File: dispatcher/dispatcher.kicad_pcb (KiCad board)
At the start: 2 copper layers, 29 parts, among them J1 Conn_01x06_Female, J2 Conn_01x18, K1 HFD2_005-S-L2-D, K2 HFD2_005-S-L2-D, U1 INA3221_Module, U2 ULN2803A, U3 ULN2803A, U5 MCP2551-I-P, U6 ChinaBluePill-bluepill-D3_Boa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

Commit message: mainboard4 ready for production
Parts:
- added C1: C, Capacitor_THT:C_Disc_D3.4mm_W2.1mm_P2.50mm, F.Cu at (234.4, 139.7)
- added C2: C, Capacitor_THT:C_Disc_D3.4mm_W2.1mm_P2.50mm, F.Cu at (247.1, 139.7)
- R5: value R -> locked
- moved K2 140.0 mm to (252.1, 66.0), turned to 180 degrees
- moved J_TR_OUT1 133.6 mm to (251.5, 45.7), turned to 180 degrees
- moved J_LED_2 114.5 mm to (227.3, 132.1), turned to -90 degrees
- moved K1 112.5 mm to (252.1, 51.4), turned to 180 degrees
- moved J1 96.6 mm to (254.0, 132.1)
- moved R7 96.6 mm to (254.0, 127.0)
- moved U5 96.6 mm to (248.9, 119.4)
- moved J_LED_1 95.2 mm to (213.3, 132.1), turned to -90 degrees
- moved R1 94.1 mm to (226.1, 120.0)
- moved R2 94.1 mm to (228.6, 120.0)
- moved R3 94.1 mm to (223.5, 120.0)
- moved R4 94.1 mm to (221.0, 120.0)
- moved R5 94.1 mm to (233.7, 127.6)
- moved R6 94.1 mm to (231.1, 127.6)
- moved J_TR_IN1 91.7 mm to (252.1, 83.2), turned to 0 degrees
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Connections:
- J2 pad 10: Net-(J2-Pad10) -> unconnected-(J2-Pad10)
- J2 pad 11: Net-(J2-Pad11) -> unconnected-(J2-Pad11)
- J2 pad 15: Net-(J2-Pad15) -> unconnected-(J2-Pad15)
- J2 pad 5: Net-(J2-Pad5) -> unconnected-(J2-Pad5)
- J2 pad 8: Net-(J2-Pad8) -> unconnected-(J2-Pad8)
- J2 pad 9: Net-(J2-Pad9) -> unconnected-(J2-Pad9)
- K1 pad 8: Net-(K1-Pad8) -> unconnected-(K1-Pad8)
- K1 pad 9: Net-(K1-Pad9) -> unconnected-(K1-Pad9)
- K2 pad 15: Net-(K2-Pad15) -> unconnected-(K2-Pad15)
- K2 pad 8: Net-(K2-Pad8) -> unconnected-(K2-Pad8)
- K2 pad 9: Net-(K2-Pad9) -> unconnected-(K2-Pad9)
- U2 pad 15: Net-(U2-Pad15) -> unconnected-(U2-Pad15)
- U3 pad 11: Net-(U3-Pad11) -> unconnected-(U3-Pad11)
- U3 pad 12: Net-(U3-Pad12) -> unconnected-(U3-Pad12)
- U3 pad 7: Net-(U3-Pad7) -> unconnected-(U3-Pad7)
- U3 pad 8: Net-(U3-Pad8) -> unconnected-(U3-Pad8)
- U5 pad 5: Net-(U5-Pad5) -> unconnected-(U5-Pad5)
- U5 pad 8: Net-(U5-Pad8) -> unconnected-(U5-Pad8)
- U6 pad 11: Net-(U6-Pad11) -> unconnected-(U6-Pad11)
- U6 pad 13: Net-(U6-Pad13) -> unconnected-(U6-Pad13)
- U6 pad 20: Net-(U6-Pad20) -> +3V3
- U6 pad 21: Net-(U6-Pad21) -> unconnected-(U6-Pad21)
- U6 pad 22: Net-(U6-Pad22) -> unconnected-(U6-Pad22)
- U6 pad 23: Net-(U6-Pad23) -> unconnected-(U6-Pad23)
- U6 pad 24: Net-(U6-Pad24) -> unconnected-(U6-Pad24)
- U6 pad 29: Net-(U6-Pad29) -> unconnected-(U6-Pad29)
- U6 pad 34: Net-(U6-Pad34) -> unconnected-(U6-Pad34)
- U6 pad 37: Net-(U6-Pad37) -> unconnected-(U6-Pad37)
- U6 pad 38: Net-(U6-Pad38) -> unconnected-(U6-Pad38)
- U6 pad 39: Net-(U6-Pad39) -> unconnected-(U6-Pad39)
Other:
- net class Default removed

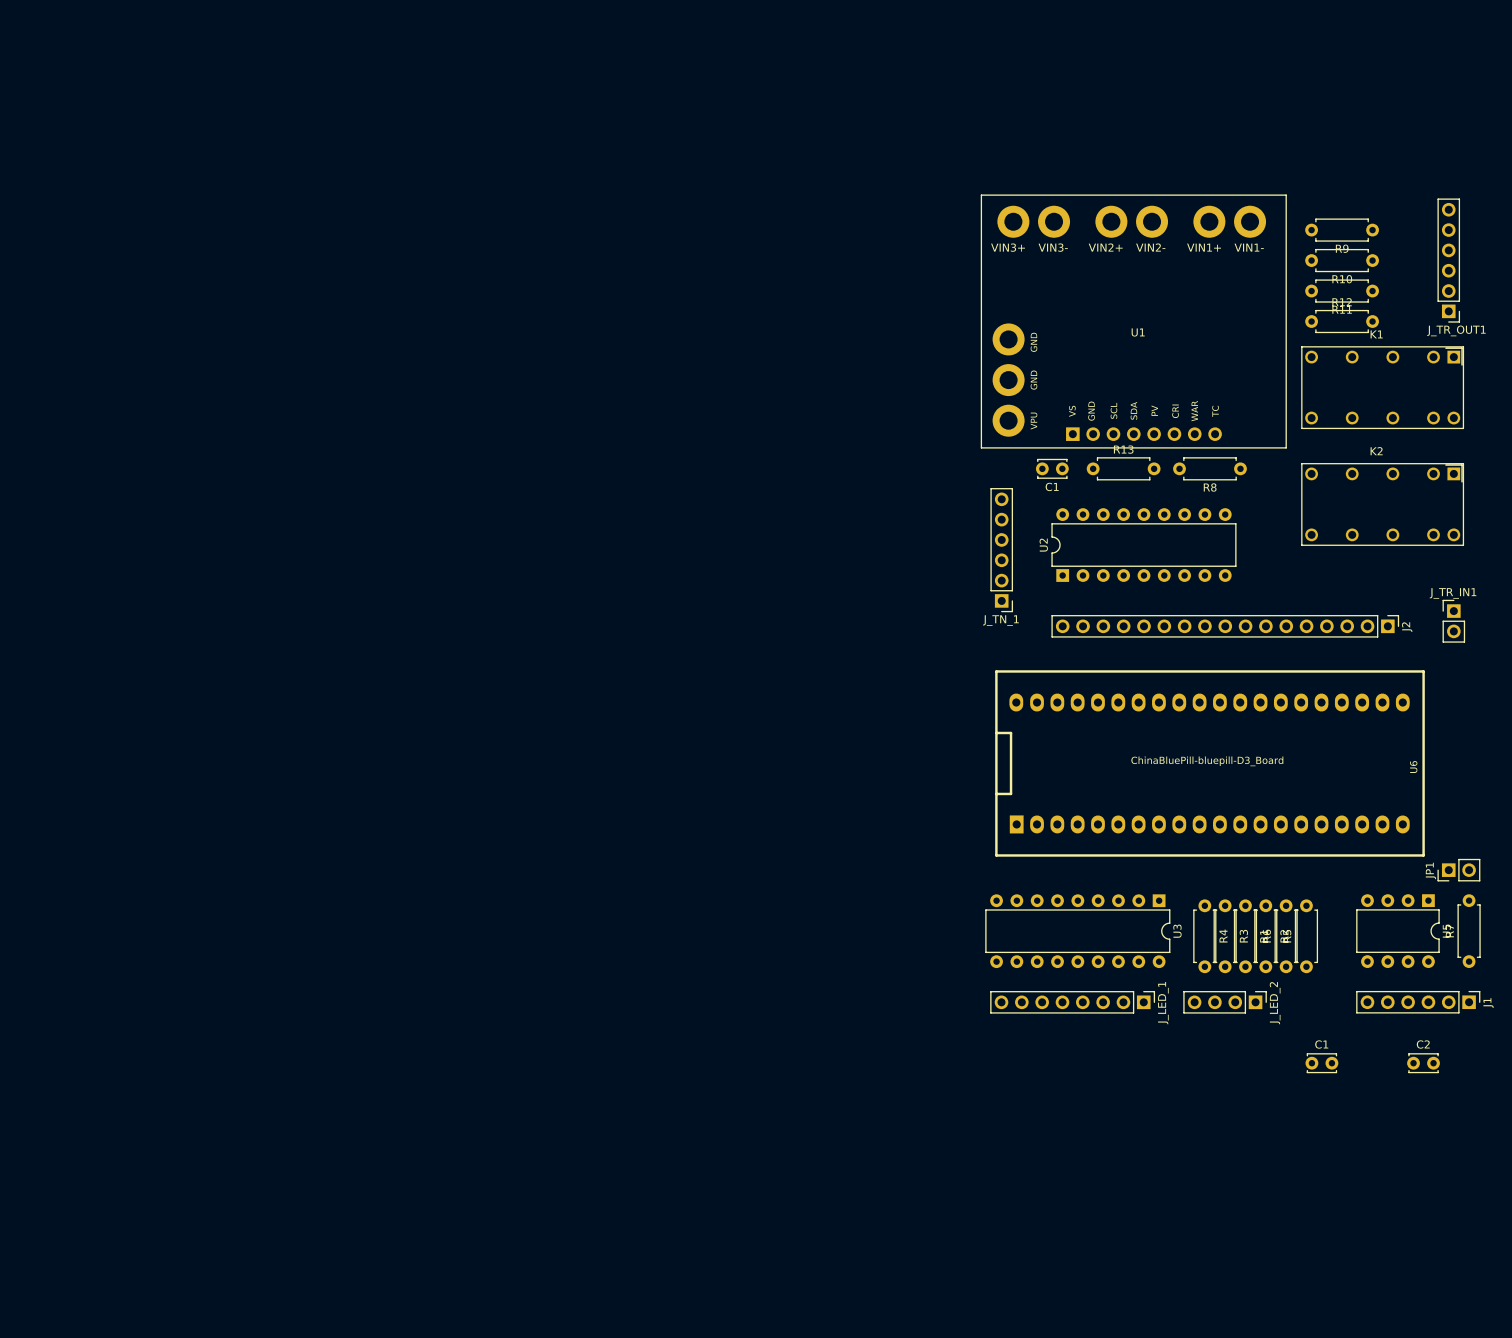
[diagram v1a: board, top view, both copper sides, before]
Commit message: updated dispatcher
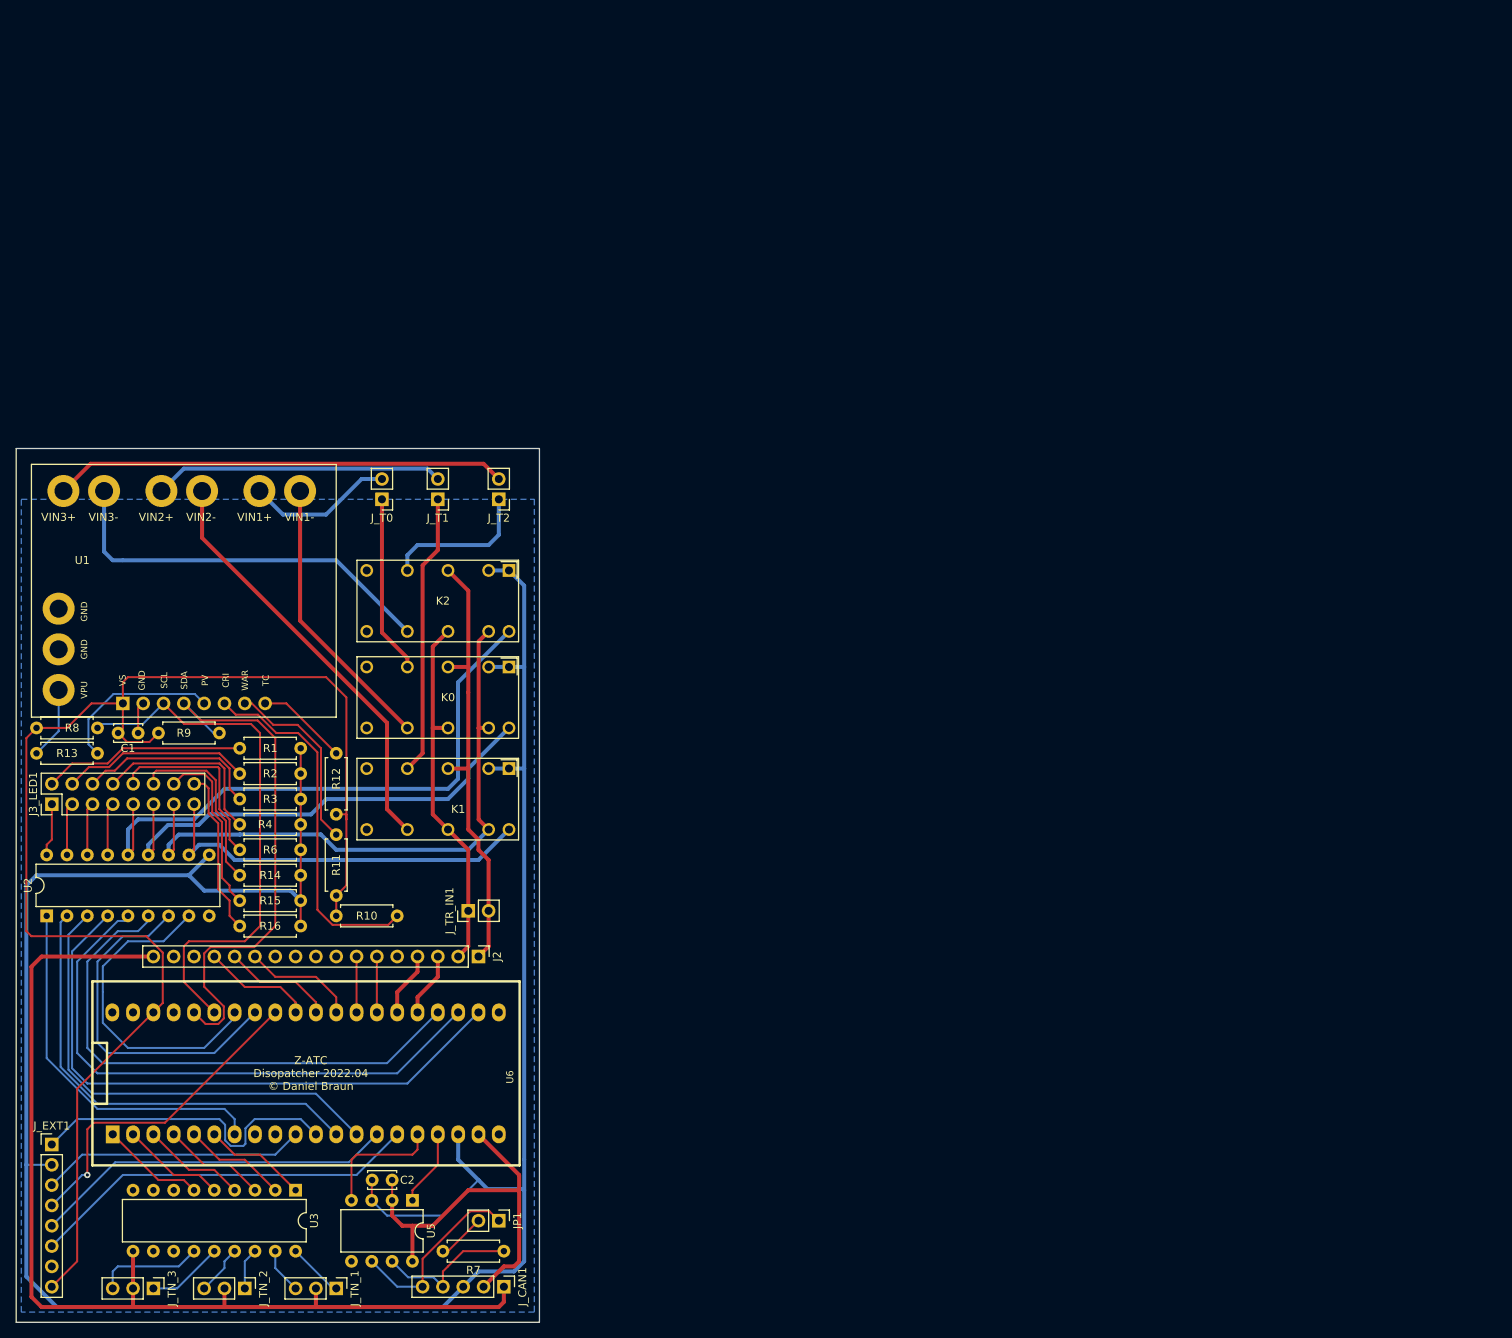
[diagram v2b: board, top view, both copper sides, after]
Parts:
- removed the C1 at (203.2, 65.4)
- removed J1, J_TR_OUT1: Conn_01x06_Female, Connector_PinHeader_2.54mm:PinHeader_1x06_P2.54mm_Vertical
- removed J_LED_1: Conn_01x08_Female, Connector_PinHeader_2.54mm:PinHeader_1x08_P2.54mm_Vertical
- removed J_LED_2: Conn_01x04_Female, Connector_PinHeader_2.54mm:PinHeader_1x04_P2.54mm_Vertical
- removed R5: locked, Resistor_THT:R_Axial_DIN0207_L6.3mm_D2.5mm_P7.62mm_Horizontal
- added J3_LED1: Conn_02x08_Odd_Even, Connector_PinHeader_2.54mm:PinHeader_2x08_P2.54mm_Vertical, F.Cu at (76.8, 107.3)
- added J_CAN1: Conn_01x05_Female, Connector_PinHeader_2.54mm:PinHeader_1x05_P2.54mm_Vertical, F.Cu at (133.3, 167.6)
- added J_EXT1: Conn_01x08_Female, Connector_PinHeader_2.54mm:PinHeader_1x08_P2.54mm_Vertical, F.Cu at (76.8, 149.9)
- added J_T0: Conn_01x02_Female, Connector_PinHeader_2.54mm:PinHeader_1x02_P2.54mm_Vertical, F.Cu at (118.1, 69.2)
- added J_T1: Conn_01x02_Female, Connector_PinHeader_2.54mm:PinHeader_1x02_P2.54mm_Vertical, F.Cu at (125.1, 69.2)
- added J_T2: Conn_01x02_Female, Connector_PinHeader_2.54mm:PinHeader_1x02_P2.54mm_Vertical, F.Cu at (132.7, 69.2)
- added J_TN_2: Conn_01x03_Female, Connector_PinHeader_2.54mm:PinHeader_1x03_P2.54mm_Vertical, F.Cu at (101.0, 167.8)
- added J_TN_3: Conn_01x03_Female, Connector_PinHeader_2.54mm:PinHeader_1x03_P2.54mm_Vertical, F.Cu at (89.5, 167.8)
- added K2: HFD2_005-S-L2-D, Modules:HFD2-005-S-L2-D, F.Cu at (134.0, 78.1)
- added R14: R, Resistor_THT:R_Axial_DIN0207_L6.3mm_D2.5mm_P7.62mm_Horizontal, F.Cu at (108.0, 116.2)
- added R15: R, Resistor_THT:R_Axial_DIN0207_L6.3mm_D2.5mm_P7.62mm_Horizontal, F.Cu at (108.0, 119.4)
- added R16: R, Resistor_THT:R_Axial_DIN0207_L6.3mm_D2.5mm_P7.62mm_Horizontal, F.Cu at (108.0, 122.6)
- J_TN_1: value Conn_01x06_Female -> Conn_01x03_Female; footprint Connector_PinHeader_2.54mm:PinHeader_1x06_P2.54mm_Vertical -> Connector_PinHeader_2.54mm:PinHeader_1x03_P2.54mm_Vertical
- moved R9 164.3 mm to (90.2, 98.4), turned to 0 degrees
- moved C1 154.8 mm to (85.1, 98.4)
- moved R10 153.3 mm to (112.4, 121.3), turned to 0 degrees
- moved R11 150.0 mm to (112.4, 118.7), turned to 90 degrees
- moved R8 146.5 mm to (82.5, 97.8)
- moved R13 136.8 mm to (74.9, 101.0)
- moved U2 133.9 mm to (76.2, 121.3)
- moved R12 133.3 mm to (112.4, 101.0), turned to -90 degrees
- moved U5 132.4 mm to (121.9, 156.8)
- moved J_TR_IN1 128.8 mm to (128.9, 120.7), turned to 90 degrees
- moved C2 128.5 mm to (119.4, 154.3), turned to 180 degrees
- moved JP1 126.6 mm to (132.7, 159.4), turned to -90 degrees
- moved R7 126.0 mm to (133.3, 163.2), turned to 180 degrees
- moved K0 124.3 mm to (134.0, 90.2)
- moved R6 124.0 mm to (108.0, 113.0), turned to 180 degrees
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- renumbered K1 to K0, K2 to K1
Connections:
- J2 pad 1: T0_0 -> TRACK0_0
- J2 pad 12: CT0_1 -> CT_0_1
- J2 pad 13: CT0_2 -> CT_0_2
- J2 pad 14: CT0_3 -> CT_0_3
- J2 pad 17: 12Vunreg -> +12V
- J_TR_IN1 pad 2: T0_0 -> TRACK0_0
- K0 pad 1: +12V -> +5V
- K0 pad 11: TT1_1 -> TT0_1
- K0 pad 15: Net-(K1-Pad15) -> Net-(J3_LED1-Pad13)
- K0 pad 16: Net-(K1-Pad16) -> Net-(J3_LED1-Pad11)
- K0 pad 2: +12V -> +5V
- K0 pad 4: T0_0 -> TRACK0_0
- K0 pad 6: T1_0 -> T0_0
- K1 pad 1: +12V -> +5V
- K1 pad 11: TT2_1 -> TT1_1
- K1 pad 15: unconnected-(K2-Pad15) -> Net-(J3_LED1-Pad13)
- K1 pad 16: Net-(K2-Pad16) -> Net-(J3_LED1-Pad15)
- K1 pad 2: +12V -> +5V
- K1 pad 4: T0_0 -> TRACK0_0
- K1 pad 6: T2_1 -> T1_0
- R1 pad 1: Net-(J_LED_1-Pad1) -> +5V
- R1 pad 2: +5V -> Net-(J3_LED1-Pad2)
- R2 pad 1: Net-(J_LED_1-Pad3) -> +5V
- R2 pad 2: +5V -> Net-(J3_LED1-Pad4)
- R3 pad 1: Net-(J_LED_1-Pad5) -> +5V
- R3 pad 2: +5V -> Net-(J3_LED1-Pad6)
- R4 pad 1: Net-(J_LED_1-Pad7) -> +5V
- R4 pad 2: +5V -> Net-(J3_LED1-Pad8)
- R6 pad 1: Net-(J_LED_2-Pad3) -> +5V
- R6 pad 2: +5V -> Net-(J3_LED1-Pad10)
- R8 pad 1: SCL -> SCL2
- R8 pad 2: GND -> +3V3
- R9 pad 1: GND -> +3V3
- R9 pad 2: SDA -> SDA2
- U1 pad 3: SCL -> SCL2
- U1 pad 4: SDA -> SDA2
- U1 pad 9: TRACK0_1 -> TT0_1
- U2 pad 1: RELAY0_0 -> LED0
- U2 pad 10: +12V -> +5V
- U2 pad 11: Net-(J_TN_1-Pad6) -> Net-(J3_LED1-Pad15)
- U2 pad 12: Net-(J_TN_1-Pad4) -> Net-(J3_LED1-Pad13)
- U2 pad 13: Net-(J_TN_1-Pad3) -> Net-(J3_LED1-Pad11)
- U2 pad 14: Net-(J_TN_1-Pad1) -> Net-(J3_LED1-Pad9)
- U2 pad 15: unconnected-(U2-Pad15) -> Net-(J3_LED1-Pad7)
- U2 pad 16: Net-(K2-Pad16) -> Net-(J3_LED1-Pad5)
- U2 pad 17: Net-(K1-Pad16) -> Net-(J3_LED1-Pad3)
- U2 pad 18: Net-(K1-Pad15) -> Net-(J3_LED1-Pad1)
- U2 pad 2: RELAY0_1 -> LED1
- U2 pad 3: RELAY1_0 -> LED2
- U2 pad 4: RELAY0_1 -> LED3
- U2 pad 5: TURN1A -> RELAY_SET2
- U2 pad 6: TURN1B -> RELAY_SET0
- U2 pad 7: TURN2A -> RELAY0
- U2 pad 8: TURN2B -> RELAY_SET1
- U2 pad 9: GND -> unconnected-(U2-Pad9)
- U3 pad 1: LED0 -> TURN1A
- U3 pad 10: +5V -> +12V
- U3 pad 17: Net-(J_LED_1-Pad4) -> Net-(J_TN_1-Pad3)
- U3 pad 18: Net-(J_LED_1-Pad2) -> Net-(J_TN_1-Pad1)
- U3 pad 2: LED1 -> TURN1B
- U3 pad 3: LED2 -> TURN2A
- U3 pad 4: LED3 -> TURN2B
- U3 pad 5: LED4 -> TURN3A
- U3 pad 6: LED5 -> TURN3B
- U5 pad 8: unconnected-(U5-Pad8) -> GND
- U6 pad 1: TURN2A -> TURN3B
- U6 pad 11: unconnected-(U6-Pad11) -> SWO
- U6 pad 12: LED5 -> LED1
- U6 pad 13: unconnected-(U6-Pad13) -> LED2
- U6 pad 14: SCL -> SCL1
- U6 pad 15: SDA -> SDA1
- U6 pad 2: TURN2B -> TURN3A
- U6 pad 20: +3V3 -> unconnected-(U6-Pad20)
- U6 pad 22: unconnected-(U6-Pad22) -> LED3
- U6 pad 23: unconnected-(U6-Pad23) -> RELAY_SET2
- U6 pad 24: unconnected-(U6-Pad24) -> RELAY_SET0
- U6 pad 28: PWM1_1 -> PWM0_2
- U6 pad 29: unconnected-(U6-Pad29) -> CT_0_1
- U6 pad 3: LED0 -> TURN2B
- U6 pad 30: RELAY0_0 -> CT_0_2
- U6 pad 31: RELAY0_1 -> CT_0_3
- U6 pad 32: RELAY1_0 -> PA7
- U6 pad 33: RELAY1_1 -> RELAY0
- U6 pad 34: unconnected-(U6-Pad34) -> RELAY_SET1
- U6 pad 35: TURN1A -> SCL2
- U6 pad 36: TURN1B -> SDA2
- U6 pad 38: unconnected-(U6-Pad38) -> +3V3
- U6 pad 39: unconnected-(U6-Pad39) -> GND
- U6 pad 4: LED1 -> TURN2A
- U6 pad 5: CT_0_3 -> TURN1B
- U6 pad 6: CT_0_2 -> TURN1A
- U6 pad 7: CT_0_1 -> LED0
- U6 pad 8: LED3 -> USB1
- U6 pad 9: LED4 -> USB2
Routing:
- net +5V: track 0.00 -> 310.3 mm
- net +3V3: track 0.00 -> 175.2 mm
- net +12V: track 0.00 -> 130.4 mm
- net Net-(J3_LED1-Pad13): track 0.00 -> 77.3 mm
- net LED3: track 0.00 -> 76.2 mm
- net Net-(J3_LED1-Pad9): track 0.00 -> 74.7 mm
- net RELAY_SET2: track 0.00 -> 72.4 mm
- net RELAY_SET0: track 0.00 -> 68.4 mm
- net SCL2: track 0.00 -> 67.7 mm
- net SDA2: track 0.00 -> 66.8 mm
- net Net-(J3_LED1-Pad11): track 0.00 -> 59.7 mm
- net LED2: track 0.00 -> 59.6 mm
- net LED1: track 0.00 -> 57.2 mm
- net T2_1: track 0.00 -> 56.6 mm
- net TRACK0_0: track 0.00 -> 56.0 mm
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- added copper zone on B.Cu, net GND
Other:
- board outline added: 65.4 x 109.2 mm
- board text added: "Z-ATC Disopatcher 2022.04 © Daniel Braun"
